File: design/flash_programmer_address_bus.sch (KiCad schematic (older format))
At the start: 6 parts, among them U501 74HC595, U502 74HC595

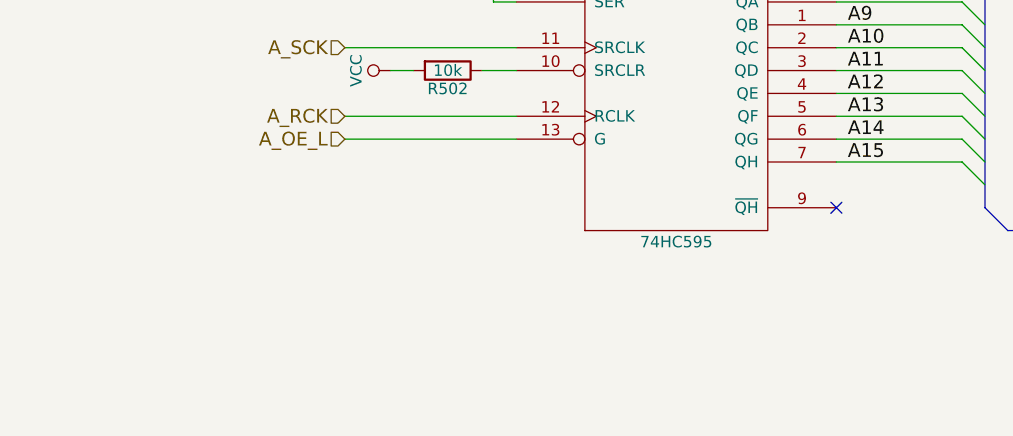
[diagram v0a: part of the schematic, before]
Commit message: Apply license to schematic files
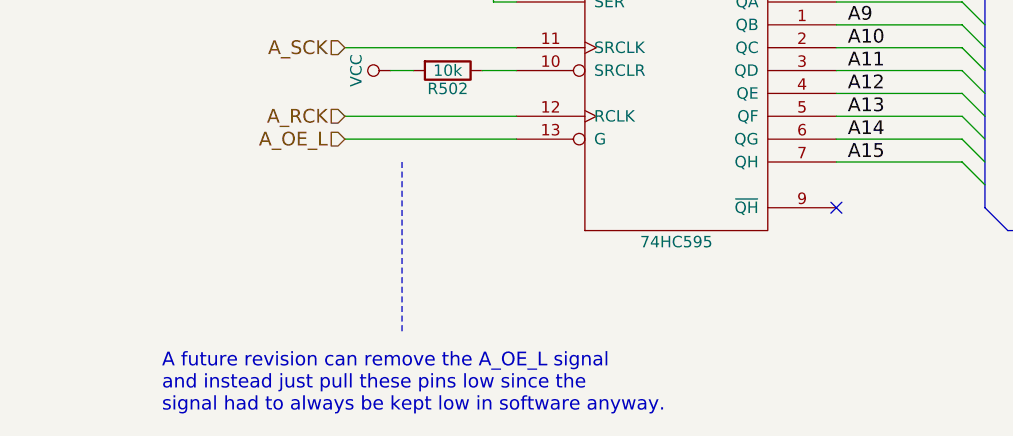
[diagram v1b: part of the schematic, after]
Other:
- note added: "A future revision can remove the A_OE_L signal\nand instead just pull these pins low since the\nsignal had to always be kept low in software anyway."
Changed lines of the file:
@@
 Date "2017-03-11"
 Rev "5"
-Comp "John DiSanti"
+Comp "Copyright 2017 John DiSanti"
 Comment1 ""
 Comment2 ""
@@
 Text Notes 8150 1600 2    118  ~ 0
 Signal Descriptions
+Wire Notes Line
+	2800 5300 2800 6050
+Text Notes 1750 6400 0    60   ~ 0
+A future revision can remove the A_OE_L signal\nand instead just pull these pins low since the\nsignal had to always be kept low in software anyway.
 $EndSCHEMATC
